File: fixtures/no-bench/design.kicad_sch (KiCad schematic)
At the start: 2 parts

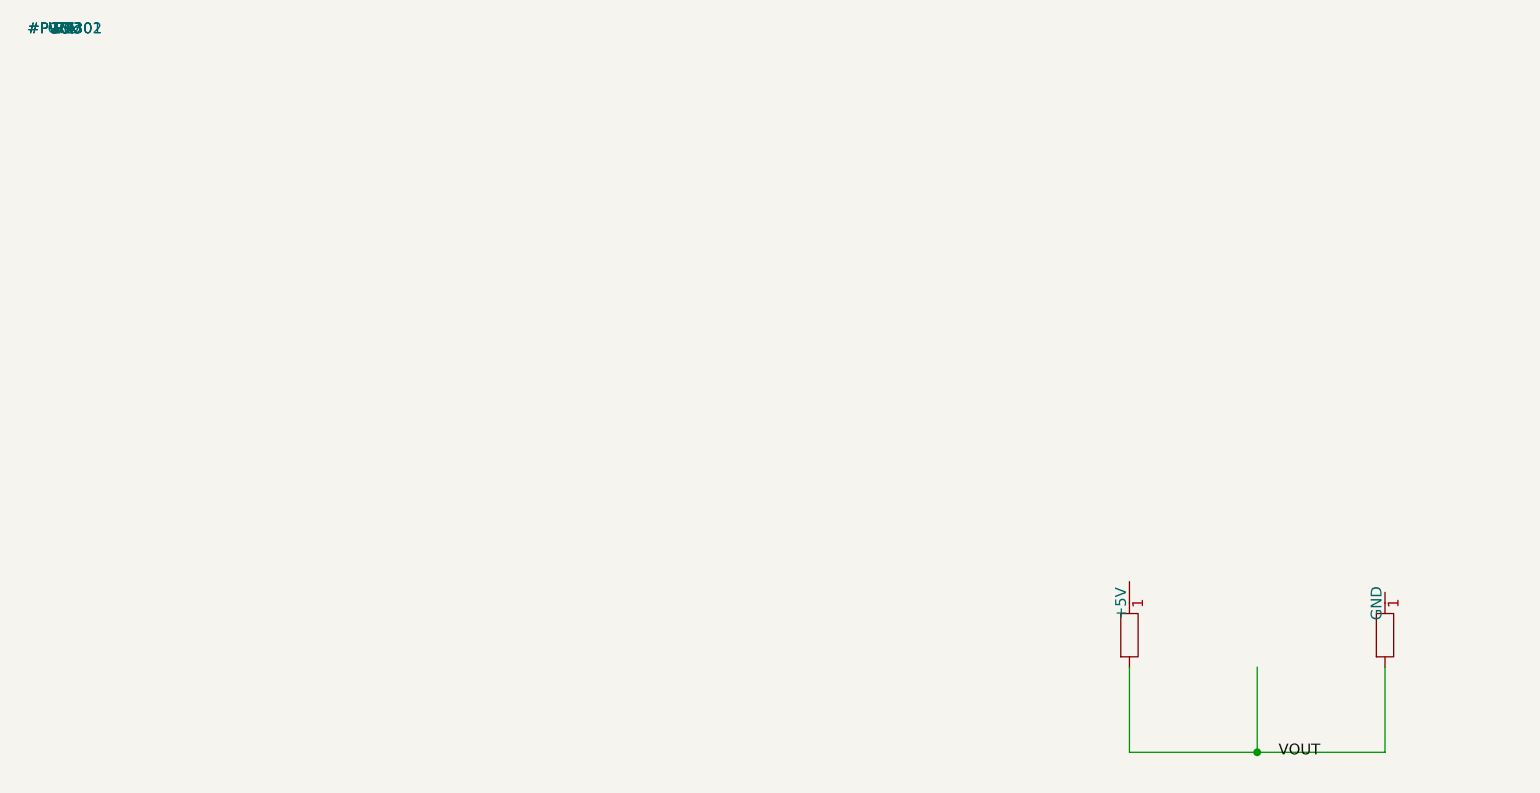
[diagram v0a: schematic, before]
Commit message: fix: фикстуры под реальный контейнер — PWR_FLAG, checks.spice инжект, ngspice без -r, путь анализатора
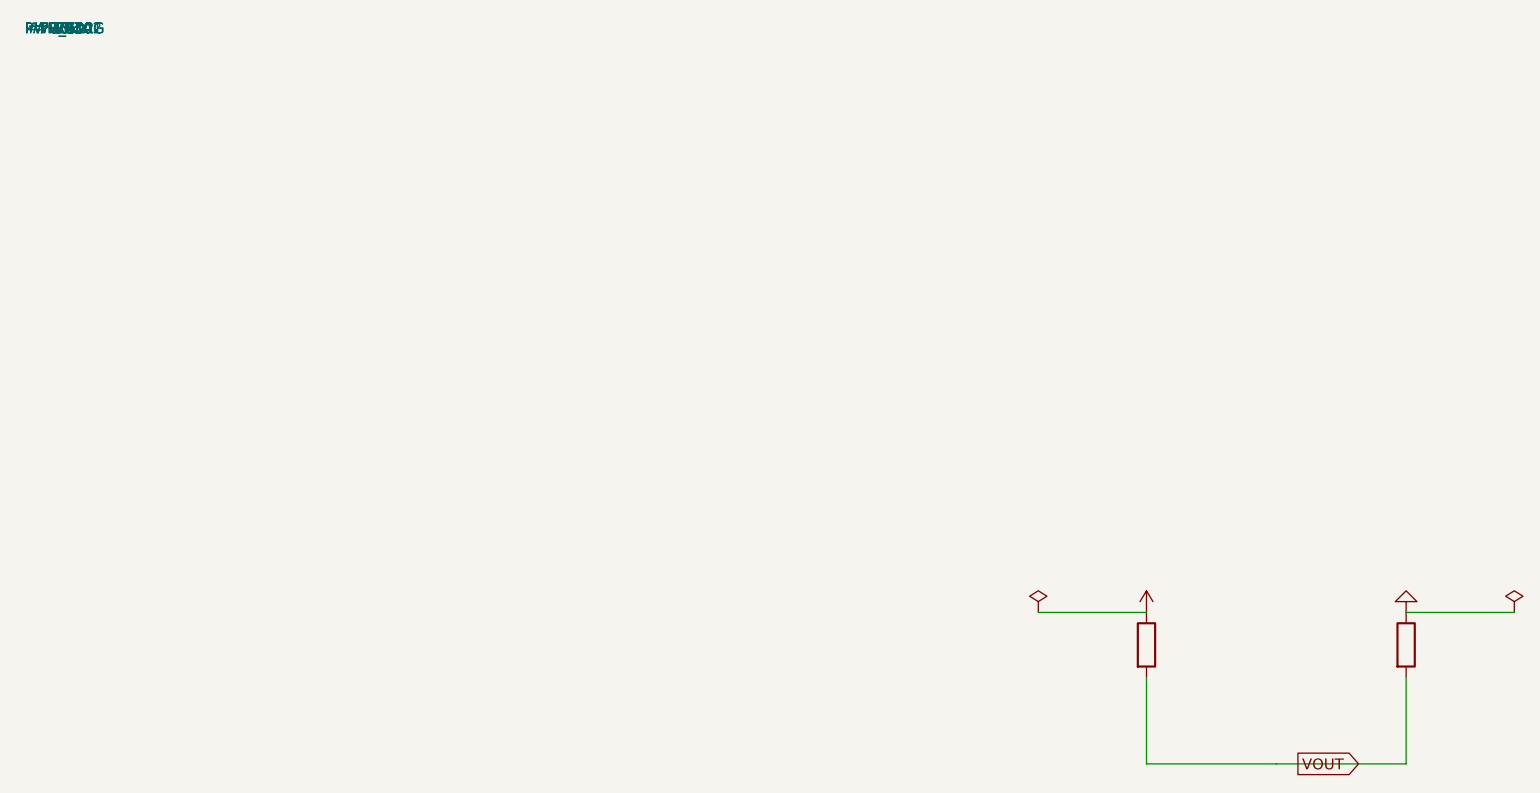
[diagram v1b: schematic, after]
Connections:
- net +5V: now also R1.1
- net GND: now also R2.1
- net VOUT: now also R1.2, R2.2
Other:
- moved on the sheet: R1, R2
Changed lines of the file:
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@@
     (title "no-bench")
   )
-  (junction (at 140 85) (diameter 0) (color 0 0 0 0))
-  (wire (pts (xy 125 75) (xy 125 85)) (stroke (width 0) (type default)))
-  (wire (pts (xy 125 85) (xy 140 85)) (stroke (width 0) (type default)))
-  (wire (pts (xy 140 75) (xy 140 85)) (stroke (width 0) (type default)))
-  (wire (pts (xy 140 85) (xy 155 85)) (stroke (width 0) (type default)))
-  (wire (pts (xy 155 75) (xy 155 85)) (stroke (width 0) (type default)))
-  (symbol (lib_id "power:+5V") (at 125 67.5 0) (unit 1)
+  (wire (pts (xy 114.3 68.58) (xy 127 68.58)) (stroke (width 0) (type default)))
+  (wire (pts (xy 127 76.2) (xy 127 86.36)) (stroke (width 0) (type default)))
+  (wire (pts (xy 127 86.36) (xy 142.24 86.36)) (stroke (width 0) (type default)))
+  (wire (pts (xy 142.24 86.36) (xy 157.48 86.36)) (stroke (width 0) (type default)))
+  (wire (pts (xy 157.48 68.58) (xy 170.18 68.58)) (stroke (width 0) (type default)))
+  (wire (pts (xy 157.48 76.2) (xy 157.48 86.36)) (stroke (width 0) (type default)))
+  (symbol (lib_id "power:+5V") (at 127 68.58 0) (unit 1)
     (property "Reference" "#PWR301")
     (property "Value" "+5V")
     (pin "1")
   )
-  (symbol (lib_id "Device:R") (at 125 71.25 0) (unit 1)
+  (symbol (lib_id "Device:R") (at 127 72.39 0) (unit 1)
     (property "Reference" "R1")
     (property "Value" "10k")
@@
     (pin "2")
   )
-  (symbol (lib_id "Device:R") (at 155 71.25 0) (unit 1)
+  (symbol (lib_id "Device:R") (at 157.48 72.39 0) (unit 1)
     (property "Reference" "R2")
     (property "Value" "10k")
@@
     (pin "2")
   )
-  (symbol (lib_id "power:GND") (at 155 67.5 180) (unit 1)
+  (symbol (lib_id "power:GND") (at 157.48 68.58 180) (unit 1)
     (property "Reference" "#PWR302")
     (property "Value" "GND")
     (pin "1")
   )
-  (label "VOUT" (at 142.5 85 0))
+  (symbol (lib_id "power:PWR_FLAG") (at 114.3 68.58 0) (unit 1)
+    (property "Reference" "#FLG01")
+    (property "Value" "PWR_FLAG")
+    (pin "1")
+  )
+  (symbol (lib_id "power:PWR_FLAG") (at 170.18 68.58 0) (unit 1)
+    (property "Reference" "#FLG02")
+    (property "Value" "PWR_FLAG")
+    (pin "1")
+  )
+  (global_label "VOUT" (shape output) (at 144.78 86.36 0)
+    (effects (font (size 1.27 1.27)) (justify left))
+  )
 )
